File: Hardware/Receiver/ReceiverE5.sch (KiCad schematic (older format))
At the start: 36 parts, among them J1 KBUS, J2 AVR-PDI-6A, J3 CONN_01X08, J4 CONN_01X06, J5 CONN_01X06, J6 CONN_01X04, J7 CONN_01X04, U1 ATXMEGA32E5-A, U2 LM2731, U3 SN74LV07A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

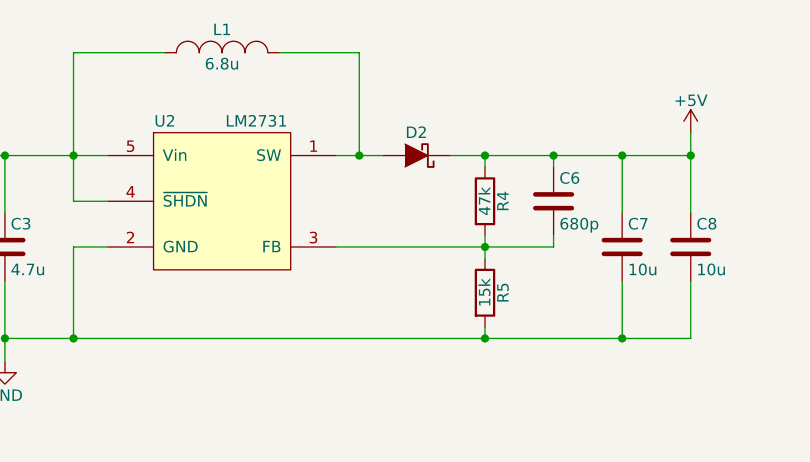
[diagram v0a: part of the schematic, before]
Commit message: Finished adding footprints
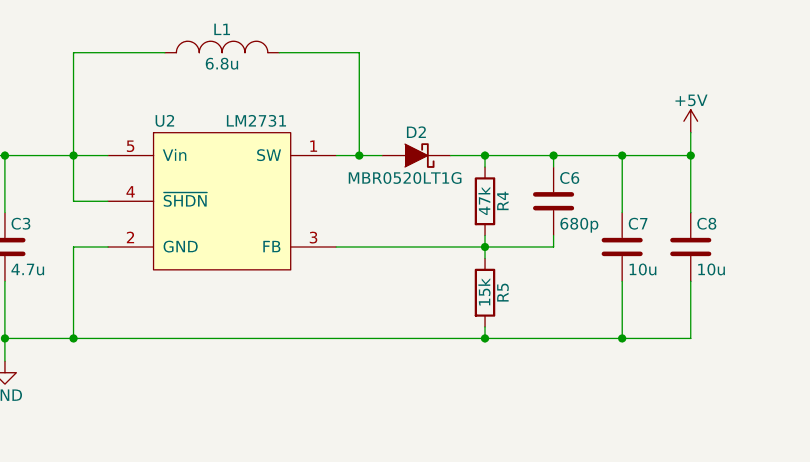
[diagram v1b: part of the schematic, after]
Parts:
- D2: value D_Schottky -> MBR0520LT1G; footprint (none) -> Diodes_SMD:SOD-123
- J1: footprint Connect:USB_A -> kuro:USB_A_multicomp
- U5: footprint (none) -> TO_SOT_Packages_SMD:SOT-23-5
- U6, U7: footprint (none) -> kuro:VSSOP8_SOT765-1
- Y1: footprint (none) -> kuro:SMD_Crystal_Multi_QC6CB_7A_ABM7
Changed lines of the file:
@@
 LIBS:valves
 LIBS:kuro
+LIBS:ReceiverE5-cache
 EELAYER 25 0
 EELAYER END
@@
 P 4900 1250
 F 0 "D2" H 4900 1150 50  0000 C CNN
-F 1 "D_Schottky" H 4900 1150 50  0001 C CNN
-F 2 "" H 4900 1250 50  0001 C CNN
+F 1 "MBR0520LT1G" H 4950 1350 50  0000 C CNN
+F 2 "Diodes_SMD:SOD-123" H 4900 1250 50  0001 C CNN
 F 3 "" H 4900 1250 50  0000 C CNN
 	1    4900 1250
@@
 F 0 "J1" V 650 1600 50  0000 C CNN
 F 1 "KBUS" V 650 1400 50  0000 C CNN
-F 2 "Connect:USB_A" V 900 1400 50  0001 C CNN
+F 2 "kuro:USB_A_multicomp" V 900 1400 50  0001 C CNN
 F 3 "" V 900 1400 50  0000 C CNN
 	1    950  1500
@@
 F 0 "U5" H 7200 1850 50  0000 C CNN
 F 1 "TPS782XX" H 7200 1750 50  0000 C CNN
-F 2 "" H 7200 1250 50  0001 C CNN
+F 2 "TO_SOT_Packages_SMD:SOT-23-5" H 7200 1250 50  0001 C CNN
 F 3 "" H 7200 1500 60  0000 C CNN
 	1    7200 1500
@@
 F 0 "U6" H 8900 4200 50  0000 C CNN
 F 1 "74LVC2T45" H 9250 4200 50  0000 C CNN
-F 2 "" H 9100 3900 60  0001 C CNN
+F 2 "kuro:VSSOP8_SOT765-1" H 9100 3900 60  0001 C CNN
 F 3 "" H 9100 3900 60  0000 C CNN
 	1    9100 3900
@@
 F 0 "U7" H 8900 5100 50  0000 C CNN
 F 1 "74LVC2T45" H 9250 5100 50  0000 C CNN
-F 2 "" H 9100 4800 60  0001 C CNN
+F 2 "kuro:VSSOP8_SOT765-1" H 9100 4800 60  0001 C CNN
 F 3 "" H 9100 4800 60  0000 C CNN
 	1    9100 4800
@@
 F 0 "Y1" H 1100 4600 50  0000 C CNN
 F 1 "Crystal" H 1100 4300 50  0000 C CNN
-F 2 "" H 1100 4450 50  0001 C CNN
+F 2 "kuro:SMD_Crystal_Multi_QC6CB_7A_ABM7" H 1100 4450 50  0001 C CNN
 F 3 "" H 1100 4450 50  0000 C CNN
 	1    1100 4450

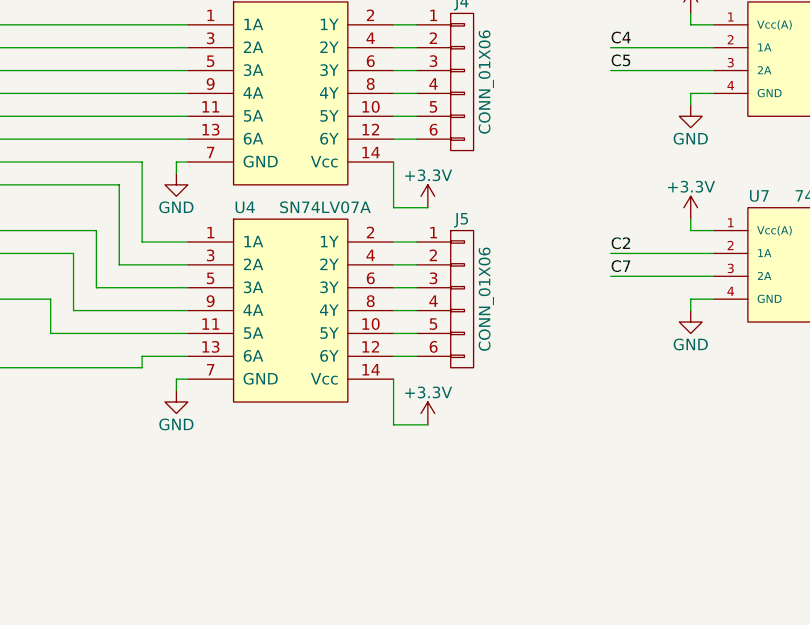
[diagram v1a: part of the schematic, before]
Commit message: Added optional MISO pull-up
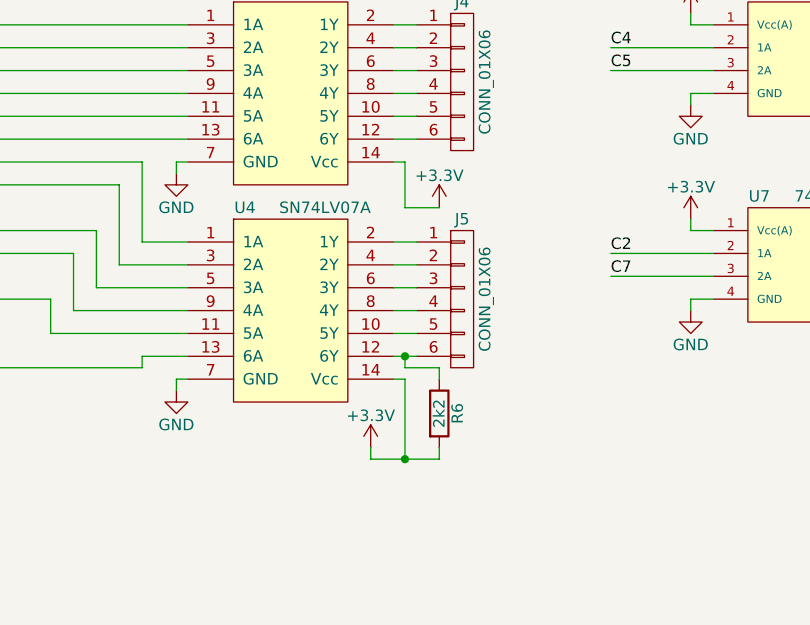
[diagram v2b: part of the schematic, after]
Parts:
- added R6: 2k2, Resistors_SMD:R_0603, symbol R
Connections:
- net +3V3: now also R6.2
- net at J5.6 (P6), U4.12 (6Y): now also R6.1
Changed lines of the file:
@@
 $EndComp
 $Comp
-L +5V #PWR01
+L +5V #PWR12
 U 1 1 582469D6
 P 6100 1150
-F 0 "#PWR01" H 6100 1000 50  0001 C CNN
+F 0 "#PWR12" H 6100 1000 50  0001 C CNN
 F 1 "+5V" H 6100 1290 50  0000 C CNN
 F 2 "" H 6100 1150 50  0000 C CNN
@@
 $EndComp
 $Comp
-L GND #PWR02
+L GND #PWR7
 U 1 1 582469FA
 P 3100 2150
-F 0 "#PWR02" H 3100 1900 50  0001 C CNN
+F 0 "#PWR7" H 3100 1900 50  0001 C CNN
 F 1 "GND" H 3100 2000 50  0000 C CNN
 F 2 "" H 3100 2150 50  0000 C CNN
@@
 $EndComp
 $Comp
-L PWR_FLAG #FLG03
+L PWR_FLAG #FLG1
 U 1 1 58246A8F
 P 10700 1350
-F 0 "#FLG03" H 10700 1445 50  0001 C CNN
+F 0 "#FLG1" H 10700 1445 50  0001 C CNN
 F 1 "PWR_FLAG" H 10700 1530 50  0000 C CNN
 F 2 "" H 10700 1350 50  0000 C CNN
@@
 $EndComp
 $Comp
-L +5V #PWR04
+L +5V #PWR32
 U 1 1 58246B44
 P 10350 1350
-F 0 "#PWR04" H 10350 1200 50  0001 C CNN
+F 0 "#PWR32" H 10350 1200 50  0001 C CNN
 F 1 "+5V" H 10350 1490 50  0000 C CNN
 F 2 "" H 10350 1350 50  0000 C CNN
@@
 $EndComp
 $Comp
-L +5V #PWR05
+L +5V #PWR5
 U 1 1 5824886A
 P 1350 1200
-F 0 "#PWR05" H 1350 1050 50  0001 C CNN
+F 0 "#PWR5" H 1350 1050 50  0001 C CNN
 F 1 "+5V" H 1350 1340 50  0000 C CNN
 F 2 "" H 1350 1200 50  0000 C CNN
@@
 $EndComp
 $Comp
-L GND #PWR06
+L GND #PWR6
 U 1 1 582489D4
 P 1350 1900
-F 0 "#PWR06" H 1350 1650 50  0001 C CNN
+F 0 "#PWR6" H 1350 1650 50  0001 C CNN
 F 1 "GND" H 1350 1750 50  0000 C CNN
 F 2 "" H 1350 1900 50  0000 C CNN
@@
 $EndComp
 $Comp
-L +5V #PWR07
+L +5V #PWR15
 U 1 1 5824ABA7
 P 6700 1300
-F 0 "#PWR07" H 6700 1150 50  0001 C CNN
+F 0 "#PWR15" H 6700 1150 50  0001 C CNN
 F 1 "+5V" H 6700 1440 50  0000 C CNN
 F 2 "" H 6700 1300 50  0000 C CNN
@@
 $EndComp
 $Comp
-L GND #PWR08
+L GND #PWR16
 U 1 1 5824AD24
 P 6700 1700
-F 0 "#PWR08" H 6700 1450 50  0001 C CNN
+F 0 "#PWR16" H 6700 1450 50  0001 C CNN
 F 1 "GND" H 6700 1550 50  0000 C CNN
 F 2 "" H 6700 1700 50  0000 C CNN
@@
 $EndComp
 $Comp
-L GND #PWR09
+L GND #PWR20
 U 1 1 5824B020
 P 7950 1700
-F 0 "#PWR09" H 7950 1450 50  0001 C CNN
+F 0 "#PWR20" H 7950 1450 50  0001 C CNN
 F 1 "GND" H 7950 1550 50  0000 C CNN
 F 2 "" H 7950 1700 50  0000 C CNN
@@
 $EndComp
 $Comp
-L +3.3V #PWR010
+L +3.3V #PWR19
 U 1 1 5824B213
 P 7950 1300
-F 0 "#PWR010" H 7950 1150 50  0001 C CNN
+F 0 "#PWR19" H 7950 1150 50  0001 C CNN
 F 1 "+3.3V" H 7950 1440 50  0000 C CNN
 F 2 "" H 7950 1300 50  0000 C CNN
@@
 $EndComp
 $Comp
-L +3.3V #PWR011
+L +3.3V #PWR33
 U 1 1 5824C026
 P 10350 1650
-F 0 "#PWR011" H 10350 1500 50  0001 C CNN
+F 0 "#PWR33" H 10350 1500 50  0001 C CNN
 F 1 "+3.3V" H 10350 1790 50  0000 C CNN
 F 2 "" H 10350 1650 50  0000 C CNN
@@
 $EndComp
 $Comp
-L PWR_FLAG #FLG012
+L PWR_FLAG #FLG2
 U 1 1 5824C328
 P 10700 1650
-F 0 "#FLG012" H 10700 1745 50  0001 C CNN
+F 0 "#FLG2" H 10700 1745 50  0001 C CNN
 F 1 "PWR_FLAG" H 10700 1830 50  0000 C CNN
 F 2 "" H 10700 1650 50  0000 C CNN
@@
 $EndComp
 $Comp
-L GND #PWR013
+L GND #PWR13
 U 1 1 5824EEE6
 P 6350 4400
-F 0 "#PWR013" H 6350 4150 50  0001 C CNN
+F 0 "#PWR13" H 6350 4150 50  0001 C CNN
 F 1 "GND" H 6350 4250 50  0000 C CNN
 F 2 "" H 6350 4400 50  0000 C CNN
@@
 $EndComp
 $Comp
-L GND #PWR014
+L GND #PWR14
 U 1 1 5824F2F5
 P 6350 5350
-F 0 "#PWR014" H 6350 5100 50  0001 C CNN
+F 0 "#PWR14" H 6350 5100 50  0001 C CNN
 F 1 "GND" H 6350 5200 50  0000 C CNN
 F 2 "" H 6350 5350 50  0000 C CNN
@@
 C5
 $Comp
-L GND #PWR015
+L GND #PWR22
 U 1 1 58251C44
 P 8600 4100
-F 0 "#PWR015" H 8600 3850 50  0001 C CNN
+F 0 "#PWR22" H 8600 3850 50  0001 C CNN
 F 1 "GND" H 8600 3950 50  0000 C CNN
 F 2 "" H 8600 4100 50  0000 C CNN
@@
 $EndComp
 $Comp
-L GND #PWR016
+L GND #PWR24
 U 1 1 58251C82
 P 8600 5000
-F 0 "#PWR016" H 8600 4750 50  0001 C CNN
+F 0 "#PWR24" H 8600 4750 50  0001 C CNN
 F 1 "GND" H 8600 4850 50  0000 C CNN
 F 2 "" H 8600 5000 50  0000 C CNN
@@
 $EndComp
 $Comp
-L +3.3V #PWR017
+L +3.3V #PWR21
 U 1 1 582523F9
 P 8600 3700
-F 0 "#PWR017" H 8600 3550 50  0001 C CNN
+F 0 "#PWR21" H 8600 3550 50  0001 C CNN
 F 1 "+3.3V" H 8600 3840 50  0000 C CNN
 F 2 "" H 8600 3700 50  0000 C CNN
@@
 $EndComp
 $Comp
-L +3.3V #PWR018
+L +3.3V #PWR23
 U 1 1 58252575
 P 8600 4600
-F 0 "#PWR018" H 8600 4450 50  0001 C CNN
+F 0 "#PWR23" H 8600 4450 50  0001 C CNN
 F 1 "+3.3V" H 8600 4740 50  0000 C CNN
 F 2 "" H 8600 4600 50  0000 C CNN
@@
 $EndComp
 $Comp
-L +5V #PWR019
+L +5V #PWR27
 U 1 1 58253B37
 P 9600 3700
-F 0 "#PWR019" H 9600 3550 50  0001 C CNN
+F 0 "#PWR27" H 9600 3550 50  0001 C CNN
 F 1 "+5V" H 9600 3840 50  0000 C CNN
 F 2 "" H 9600 3700 50  0000 C CNN
@@
 $EndComp
 $Comp
-L GND #PWR020
+L GND #PWR29
 U 1 1 58254196
 P 9600 5000
-F 0 "#PWR020" H 9600 4750 50  0001 C CNN
+F 0 "#PWR29" H 9600 4750 50  0001 C CNN
 F 1 "GND" H 9600 4850 50  0000 C CNN
 F 2 "" H 9600 5000 50  0000 C CNN
@@
 $EndComp
 $Comp
-L +5V #PWR021
+L +5V #PWR28
 U 1 1 582542A3
 P 9600 4600
-F 0 "#PWR021" H 9600 4450 50  0001 C CNN
+F 0 "#PWR28" H 9600 4450 50  0001 C CNN
 F 1 "+5V" H 9600 4740 50  0000 C CNN
 F 2 "" H 9600 4600 50  0000 C CNN
@@
 $EndComp
 $Comp
-L +3.3V #PWR022
+L +3.3V #PWR18
 U 1 1 5825A872
-P 7450 4550
-F 0 "#PWR022" H 7450 4400 50  0001 C CNN
-F 1 "+3.3V" H 7450 4690 50  0000 C CNN
-F 2 "" H 7450 4550 50  0000 C CNN
-F 3 "" H 7450 4550 50  0000 C CNN
-	1    7450 4550
-	1    0    0    -1
-$EndComp
-$Comp
-L +3.3V #PWR023
+P 7500 4550
+F 0 "#PWR18" H 7500 4400 50  0001 C CNN
+F 1 "+3.3V" H 7500 4690 50  0000 C CNN
+F 2 "" H 7500 4550 50  0000 C CNN
+F 3 "" H 7500 4550 50  0000 C CNN
+	1    7500 4550
+	1    0    0    -1
+$EndComp
+$Comp
+L +3.3V #PWR17
 U 1 1 5825A961
-P 7450 5500
-F 0 "#PWR023" H 7450 5350 50  0001 C CNN
-F 1 "+3.3V" H 7450 5640 50  0000 C CNN
-F 2 "" H 7450 5500 50  0000 C CNN
-F 3 "" H 7450 5500 50  0000 C CNN
-	1    7450 5500
+P 7200 5600
+F 0 "#PWR17" H 7200 5450 50  0001 C CNN
+F 1 "+3.3V" H 7200 5740 50  0000 C CNN
+F 2 "" H 7200 5600 50  0000 C CNN
+F 3 "" H 7200 5600 50  0000 C CNN
+	1    7200 5600
 	1    0    0    -1
 $EndComp
@@
 $EndComp
 $Comp
-L +5V #PWR024
+L +5V #PWR30
 U 1 1 5825BCEC
 P 10300 5500
-F 0 "#PWR024" H 10300 5350 50  0001 C CNN
+F 0 "#PWR30" H 10300 5350 50  0001 C CNN
 F 1 "+5V" H 10300 5640 50  0000 C CNN
 F 2 "" H 10300 5500 50  0000 C CNN
@@
 $EndComp
 $Comp
-L GND #PWR025
+L GND #PWR31
 U 1 1 5825BEA2
 P 10300 5900
-F 0 "#PWR025" H 10300 5650 50  0001 C CNN
+F 0 "#PWR31" H 10300 5650 50  0001 C CNN
 F 1 "GND" H 10300 5750 50  0000 C CNN
 F 2 "" H 10300 5900 50  0000 C CNN
@@
 $EndComp
 $Comp
-L GND #PWR026
+L GND #PWR1
 U 1 1 5825FD90
 P 750 5000
-F 0 "#PWR026" H 750 4750 50  0001 C CNN
+F 0 "#PWR1" H 750 4750 50  0001 C CNN
 F 1 "GND" H 750 4850 50  0000 C CNN
 F 2 "" H 750 5000 50  0000 C CNN
@@
 $EndComp
 $Comp
-L GND #PWR027
+L GND #PWR3
 U 1 1 582615C7
 P 1100 3650
-F 0 "#PWR027" H 1100 3400 50  0001 C CNN
+F 0 "#PWR3" H 1100 3400 50  0001 C CNN
 F 1 "GND" H 1100 3500 50  0000 C CNN
 F 2 "" H 1100 3650 50  0000 C CNN
@@
 $EndComp
 $Comp
-L +3.3V #PWR028
+L +3.3V #PWR2
 U 1 1 582618AA
 P 900 3800
-F 0 "#PWR028" H 900 3650 50  0001 C CNN
+F 0 "#PWR2" H 900 3650 50  0001 C CNN
 F 1 "+3.3V" H 900 3940 50  0000 C CNN
 F 2 "" H 900 3800 50  0000 C CNN
@@
 $EndComp
 $Comp
-L +3.3V #PWR029
+L +3.3V #PWR8
 U 1 1 58261F69
 P 3600 2800
-F 0 "#PWR029" H 3600 2650 50  0001 C CNN
+F 0 "#PWR8" H 3600 2650 50  0001 C CNN
 F 1 "+3.3V" H 3600 2940 50  0000 C CNN
 F 2 "" H 3600 2800 50  0000 C CNN
@@
 $EndComp
 $Comp
-L GND #PWR030
+L GND #PWR9
 U 1 1 582625C0
 P 3800 3250
-F 0 "#PWR030" H 3800 3000 50  0001 C CNN
+F 0 "#PWR9" H 3800 3000 50  0001 C CNN
 F 1 "GND" H 3800 3100 50  0000 C CNN
 F 2 "" H 3800 3250 50  0000 C CNN
@@
 $EndComp
 $Comp
-L GND #PWR031
+L GND #PWR11
 U 1 1 58262CE9
 P 4300 3250
-F 0 "#PWR031" H 4300 3000 50  0001 C CNN
+F 0 "#PWR11" H 4300 3000 50  0001 C CNN
 F 1 "GND" H 4300 3100 50  0000 C CNN
 F 2 "" H 4300 3250 50  0000 C CNN
@@
 $EndComp
 $Comp
-L GND #PWR032
+L GND #PWR10
 U 1 1 58264117
 P 3850 5800
-F 0 "#PWR032" H 3850 5550 50  0001 C CNN
+F 0 "#PWR10" H 3850 5550 50  0001 C CNN
 F 1 "GND" H 3850 5650 50  0000 C CNN
 F 2 "" H 3850 5800 50  0000 C CNN
@@
 OPT2
 $Comp
-L GND #PWR033
+L GND #PWR4
 U 1 1 582674C6
 P 1300 6800
-F 0 "#PWR033" H 1300 6550 50  0001 C CNN
+F 0 "#PWR4" H 1300 6550 50  0001 C CNN
 F 1 "GND" H 1300 6650 50  0000 C CNN
 F 2 "" H 1300 6800 50  0000 C CNN
@@
 Wire Wire Line
 	7300 5200 7400 5200
-Wire Wire Line
-	7300 4350 7300 4550
-Wire Wire Line
-	7300 4550 7450 4550
-Wire Wire Line
-	7300 5300 7300 5500
-Wire Wire Line
-	7300 5500 7450 5500
 Wire Wire Line
 	9500 3850 10450 3850
@@
 Connection ~ 6100 1250
 $Comp
-L +3.3V #PWR034
+L +3.3V #PWR25
 U 1 1 5827EBCB
 P 8700 1200
-F 0 "#PWR034" H 8700 1050 50  0001 C CNN
+F 0 "#PWR25" H 8700 1050 50  0001 C CNN
 F 1 "+3.3V" H 8700 1340 50  0000 C CNN
 F 2 "" H 8700 1200 50  0000 C CNN
@@
 Connection ~ 9000 1650
 $Comp
-L GND #PWR035
+L GND #PWR26
 U 1 1 5827F399
 P 8700 1700
-F 0 "#PWR035" H 8700 1450 50  0001 C CNN
+F 0 "#PWR26" H 8700 1450 50  0001 C CNN
 F 1 "GND" H 8700 1550 50  0000 C CNN
 F 2 "" H 8700 1700 50  0000 C CNN
@@
 $EndComp
 Connection ~ 8700 1650
+$Comp
+L R R6
+U 1 1 582A684B
+P 7500 5450
+F 0 "R6" V 7580 5450 50  0000 C CNN
+F 1 "2k2" V 7500 5450 50  0000 C CNN
+F 2 "Resistors_SMD:R_0603" V 7430 5450 50  0001 C CNN
+F 3 "" H 7500 5450 50  0000 C CNN
+	1    7500 5450
+	1    0    0    -1
+$EndComp
+Wire Wire Line
+	7350 5200 7350 5250
+Wire Wire Line
+	7350 5250 7500 5250
+Connection ~ 7350 5200
+Wire Wire Line
+	7500 5250 7500 5300
+Wire Wire Line
+	7300 5300 7350 5300
+Wire Wire Line
+	7350 5300 7350 5650
+Wire Wire Line
+	7500 5650 7500 5600
+Wire Wire Line
+	7200 5650 7500 5650
+Wire Wire Line
+	7200 5650 7200 5600
+Connection ~ 7350 5650
+Wire Wire Line
+	7500 4550 7350 4550
+Wire Wire Line
+	7350 4550 7350 4350
+Wire Wire Line
+	7350 4350 7300 4350
 $EndSCHEMATC
